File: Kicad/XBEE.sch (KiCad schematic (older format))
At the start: 0 parts

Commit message: 
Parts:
- added M?: __XBEE-PRO, xbee_r1-XBEE-PRO, symbol __XBEE-PRO
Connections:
- new net +3.3V: M?.1 (VCC), M?.14 (VREF)
- new net GND: M?.10 (GND)
- no-connect marks 0 -> 11
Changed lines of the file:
@@
 LIBS:__xbee-pro
 LIBS:CAR
+LIBS:car_v3-cache
 EELAYER 27 0
 EELAYER END
 $Descr A4 11693 8268
 encoding utf-8
-Sheet 1 14
+Sheet 8 14
 Title ""
-Date "30 may 2014"
+Date "31 may 2014"
 Rev ""
 Comp ""
@@
 Comment4 ""
 $EndDescr
+$Comp
+L __XBEE-PRO M?
+U 1 1 538988F6
+P 5750 3700
+F 0 "M?" H 5450 4850 50  0000 L BNN
+F 1 "__XBEE-PRO" H 5550 2750 50  0000 L BNN
+F 2 "xbee_r1-XBEE-PRO" H 5850 2900 50  0001 C CNN
+F 3 "~" H 5750 3700 60  0000 C CNN
+	1    5750 3700
+	1    0    0    -1
+$EndComp
+$Comp
+L GND #PWR?
+U 1 1 5389890A
+P 4950 4450
+F 0 "#PWR?" H 4950 4450 30  0001 C CNN
+F 1 "GND" H 4950 4380 30  0001 C CNN
+F 2 "" H 4950 4450 60  0000 C CNN
+F 3 "" H 4950 4450 60  0000 C CNN
+	1    4950 4450
+	1    0    0    -1
+$EndComp
+Wire Wire Line
+	4950 4450 4950 4350
+$Comp
+L +3.3V #PWR?
+U 1 1 5389891E
+P 4950 2950
+F 0 "#PWR?" H 4950 2910 30  0001 C CNN
+F 1 "+3.3V" H 4950 3060 30  0000 C CNN
+F 2 "" H 4950 2950 60  0000 C CNN
+F 3 "" H 4950 2950 60  0000 C CNN
+	1    4950 2950
+	1    0    0    -1
+$EndComp
+Wire Wire Line
+	4950 2950 4950 3000
+NoConn ~ 6650 3000
+NoConn ~ 6650 3150
+NoConn ~ 6650 3300
+NoConn ~ 6650 3450
+NoConn ~ 6650 3750
+NoConn ~ 6650 3600
+$Comp
+L +3.3V #PWR?
+U 1 1 53898952
+P 6750 3850
+F 0 "#PWR?" H 6750 3810 30  0001 C CNN
+F 1 "+3.3V" H 6750 3960 30  0000 C CNN
+F 2 "" H 6750 3850 60  0000 C CNN
+F 3 "" H 6750 3850 60  0000 C CNN
+	1    6750 3850
+	1    0    0    -1
+$EndComp
+Wire Wire Line
+	6750 3850 6750 3900
+Wire Wire Line
+	6750 3900 6650 3900
+NoConn ~ 4950 3750
+NoConn ~ 4950 3900
+NoConn ~ 4950 3450
+NoConn ~ 6650 4200
+NoConn ~ 6650 4350
 $EndSCHEMATC

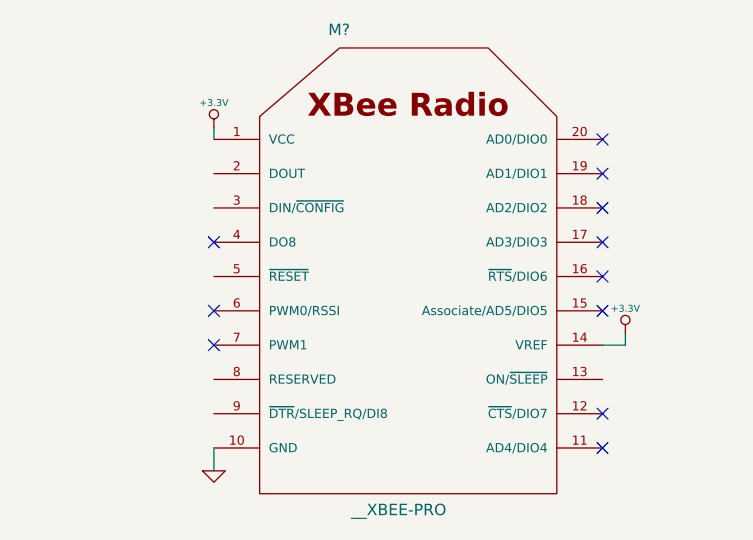
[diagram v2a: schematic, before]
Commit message: 
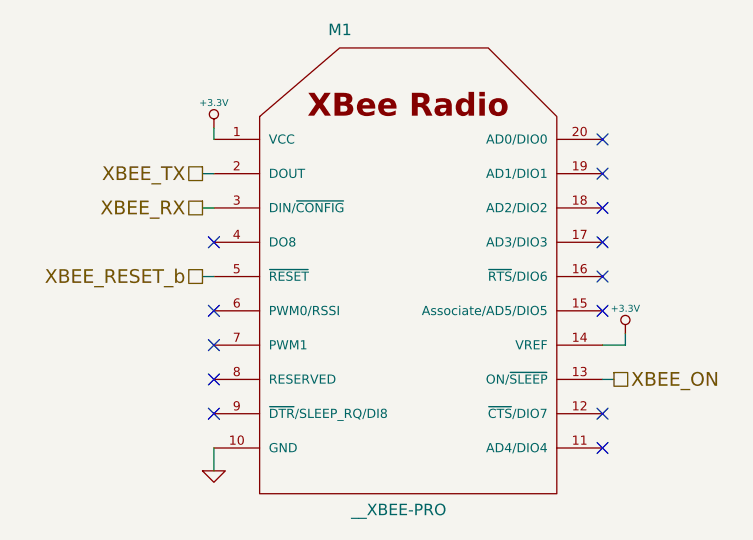
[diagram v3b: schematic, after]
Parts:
- gave numbers to parts that had none: 1
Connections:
- net XBEE_ON: now reaches M1.13 (ON/~SLEEP)
- net XBEE_TX: now reaches M1.2 (DOUT)
- net XBEE_RX: now reaches M1.3 (DIN/~CONFIG)
- net XBEE_RESET_b: now reaches M1.5 (~RESET)
- no-connect marks 11 -> 13
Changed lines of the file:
@@
 $Descr A4 11693 8268
 encoding utf-8
-Sheet 8 14
+Sheet 8 15
 Title ""
 Date "1 jun 2014"
@@
 $EndDescr
 $Comp
-L __XBEE-PRO M?
+L __XBEE-PRO M1
 U 1 1 538988F6
 P 5750 3700
-F 0 "M?" H 5450 4850 50  0000 L BNN
+F 0 "M1" H 5450 4850 50  0000 L BNN
 F 1 "__XBEE-PRO" H 5550 2750 50  0000 L BNN
 F 2 "xbee_r1-XBEE-PRO" H 5850 2900 50  0001 C CNN
@@
 $EndComp
 $Comp
-L GND #PWR?
+L GND #PWR051
 U 1 1 5389890A
 P 4950 4450
-F 0 "#PWR?" H 4950 4450 30  0001 C CNN
+F 0 "#PWR051" H 4950 4450 30  0001 C CNN
 F 1 "GND" H 4950 4380 30  0001 C CNN
 F 2 "" H 4950 4450 60  0000 C CNN
@@
 	4950 4450 4950 4350
 $Comp
-L +3.3V #PWR?
+L +3.3V #PWR052
 U 1 1 5389891E
 P 4950 2950
-F 0 "#PWR?" H 4950 2910 30  0001 C CNN
+F 0 "#PWR052" H 4950 2910 30  0001 C CNN
 F 1 "+3.3V" H 4950 3060 30  0000 C CNN
 F 2 "" H 4950 2950 60  0000 C CNN
@@
 NoConn ~ 6650 3600
 $Comp
-L +3.3V #PWR?
+L +3.3V #PWR053
 U 1 1 53898952
 P 6750 3850
-F 0 "#PWR?" H 6750 3810 30  0001 C CNN
+F 0 "#PWR053" H 6750 3810 30  0001 C CNN
 F 1 "+3.3V" H 6750 3960 30  0000 C CNN
 F 2 "" H 6750 3850 60  0000 C CNN
@@
 NoConn ~ 6650 4200
 NoConn ~ 6650 4350
+NoConn ~ 4950 4050
+NoConn ~ 4950 4200
+Text HLabel 6700 4050 2    60   UnSpc ~ 0
+XBEE_ON
+Text HLabel 4900 3600 0    60   UnSpc ~ 0
+XBEE_RESET_b
+Text HLabel 4900 3300 0    60   UnSpc ~ 0
+XBEE_RX
+Text HLabel 4900 3150 0    60   UnSpc ~ 0
+XBEE_TX
+Wire Wire Line
+	4900 3150 4950 3150
+Wire Wire Line
+	4900 3300 4950 3300
+Wire Wire Line
+	4900 3600 4950 3600
+Wire Wire Line
+	6700 4050 6650 4050
 $EndSCHEMATC
